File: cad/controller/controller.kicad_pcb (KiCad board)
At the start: 2 copper layers, 95 x 80 mm, 105 parts, among them J1 RJ45_jack_POE, J2 Barrel_Jack, J3 Conn_02x03_Odd_Even, J4 Conn_01x02, J5 Conn_01x04, J6 Conn_01x05, J7 6P6C, SW1 SW_Push, SW2 SW_Push, U1 NCP1117-5.0_SOT223, U2 NCP1117-3.3_SOT223, U3 CAT811STBI-GT3, U4 W5500, U5 ATmega328-PU, U6 PCA9517A, U7 TXB0104D, Y1 25MHz, Y2 18MHz

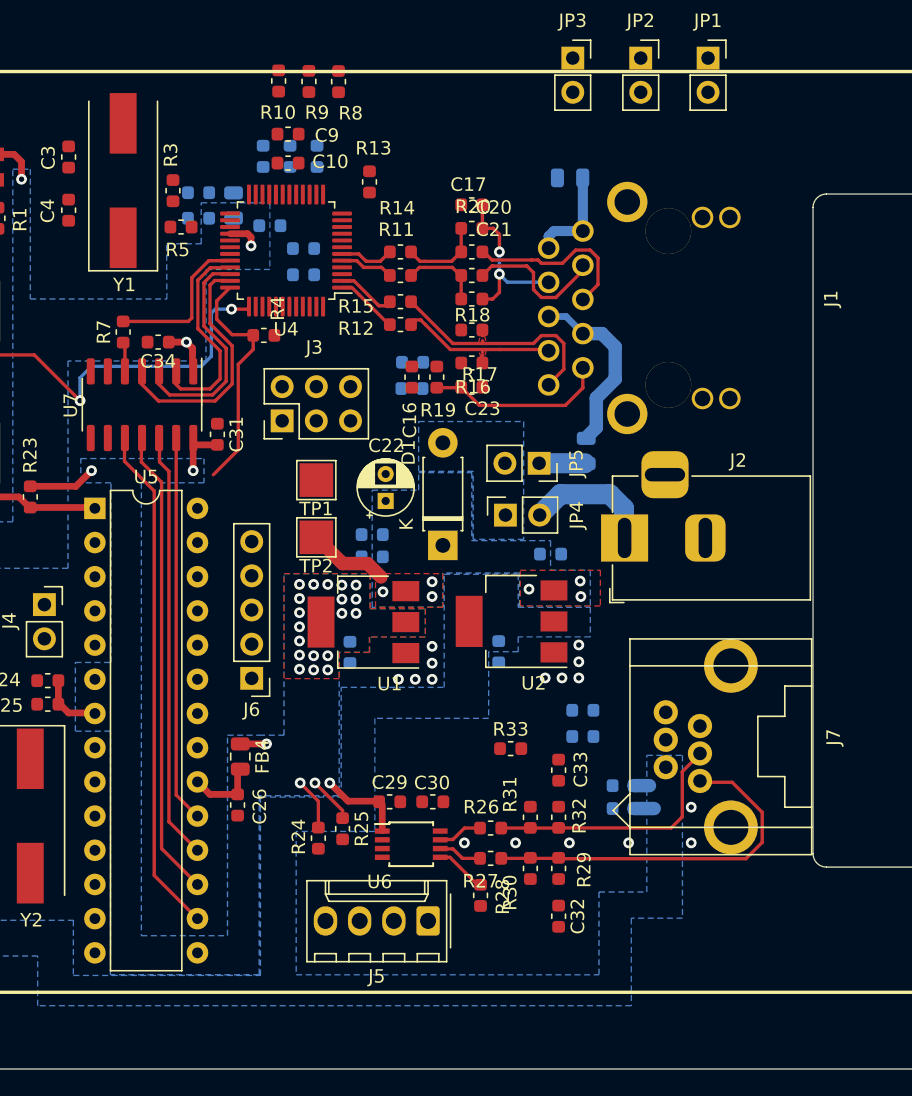
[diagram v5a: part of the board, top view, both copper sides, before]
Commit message: Continued routing controller board
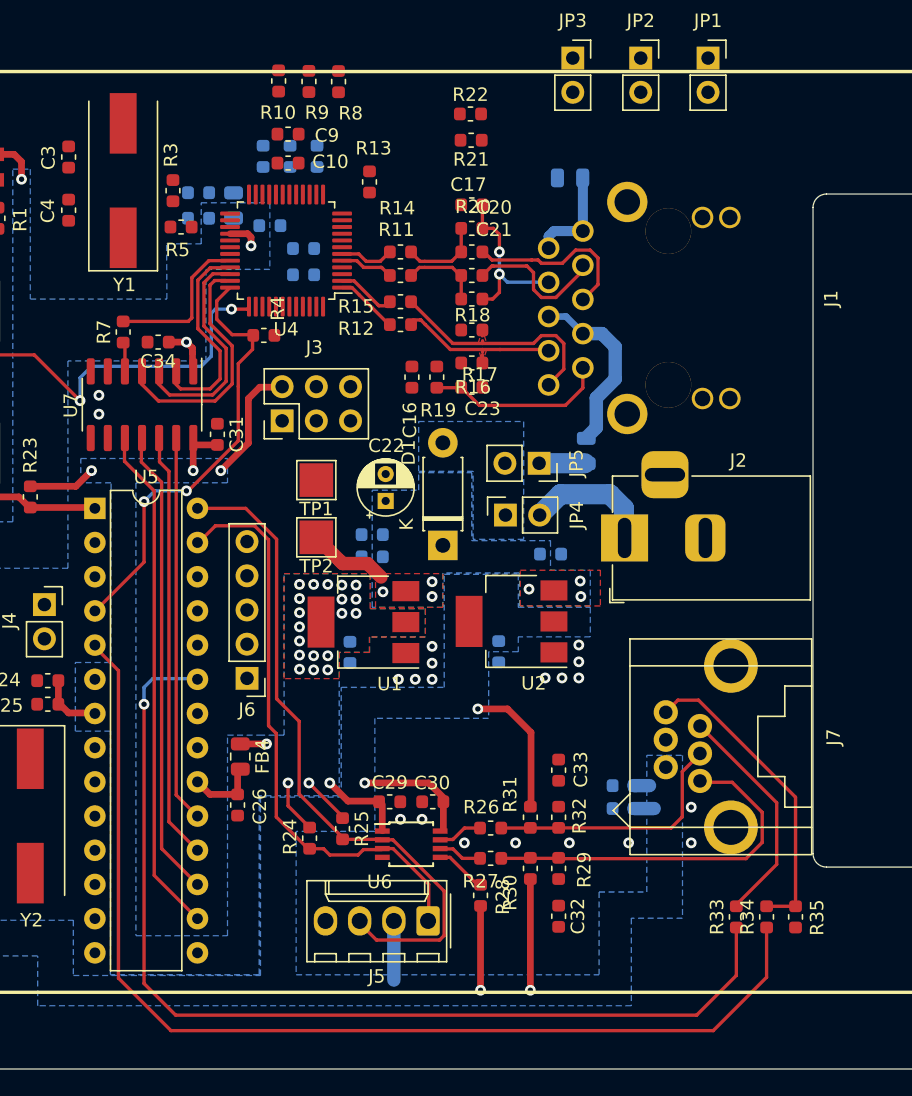
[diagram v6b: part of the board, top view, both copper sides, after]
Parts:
- R21, R22, R34, R35: moved to F.Cu
- moved R35 22.0 mm to (163.9, 113.0), turned to 90 degrees
- moved R33 20.9 mm to (159.6, 113.0), turned to 90 degrees
- moved R22 20.9 mm to (139.8, 53.4)
- moved R34 19.1 mm to (161.8, 113.0), turned to 90 degrees
- moved R21 17.1 mm to (139.8, 55.3)
- moved R24 0.65 mm to (127.8, 107.2)
- moved J6 0.35 mm to (123.2, 95.3)
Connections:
- R4 pad 1: /INT_W5500 -> INT_W5500
- U4 pad 36: /INT_W5500 -> INT_W5500
- U5 pad 4: /MCU/INT_W5500 -> INT_W5500
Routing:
- net /MCU/INT_SPARE: track 0.00 -> 80.6 mm
- net /MCU/ADC_0: track 0.00 -> 76.0 mm, vias 0 -> 1
- net /MCU/SCL: track 0.00 -> 50.2 mm
- net /MCU/SDA: track 0.00 -> 43.5 mm
- net 3V3: track 11.8 -> 49.7 mm, vias 3 -> 7
- net INT_W5500: track 0.00 -> 32.7 mm, vias 0 -> 2
- net Net-(J7-Pad1): track 0.00 -> 23.4 mm
- net /INT_W5500: track 17.5 -> 0.00 mm
- net Net-(J7-Pad2): track 0.00 -> 17.2 mm
- net 5V0: track 29.8 -> 39.1 mm, vias 25 -> 26
- net GND: vias 11 -> 13
- net (no net): vias 5 -> 7

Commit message: Continued routing controller
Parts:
- C16: moved to B.Cu
- moved J3 42.8 mm to (123.3, 118.8)
- moved C16 14.3 mm to (126.7, 61.6), turned to 0 degrees
- moved J5 5.28 mm to (140.2, 117.2)
- moved C8 2.76 mm to (123.8, 64.2), turned to 90 degrees
- moved R13 2.55 mm to (132.3, 61.0)
- moved C3 1.07 mm to (110.5, 57.5)
- moved R5 0.87 mm to (118.7, 62.5)
- moved C15 0.83 mm to (126.7, 65.0)
- moved R3 0.82 mm to (117.9, 59.9)
- moved Y1 0.81 mm to (114.2, 59.1)
- moved C14 0.75 mm to (126.7, 63.3)
- moved C11 0.60 mm to (124.4, 55.9)
- moved C12 0.60 mm to (126.4, 55.9)
- moved C13 0.60 mm to (128.4, 55.9)
- moved C10 0.55 mm to (126.2, 56.5)
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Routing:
- net RST: track 31.9 -> 83.2 mm
- net INT_W5500: track 32.7 -> 56.9 mm, vias 2 -> 0
- net /MCU/MOSI_5V: track 35.0 -> 54.3 mm
- net /3V3_ANA: track 0.00 -> 17.4 mm, vias 0 -> 8
- net /MCU/SCLK_5V: track 28.7 -> 45.7 mm
- net Net-(C3-Pad1): track 0.00 -> 16.9 mm
- net /MCU/MISO_5V: track 31.8 -> 44.6 mm
- net Net-(C4-Pad2): track 0.00 -> 11.7 mm
- net 5V0: track 39.1 -> 31.3 mm, vias 26 -> 25
- net /MCU/TX: track 0.00 -> 6.92 mm
- net /MCU/RX: track 0.00 -> 6.60 mm
- net /MCU/ADC_0: track 76.0 -> 82.4 mm
- net /MCU/SCL: track 50.2 -> 55.7 mm
- net /MCU/SDA: track 43.5 -> 48.5 mm
- net Net-(C9-Pad1): track 0.00 -> 4.99 mm
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- added copper zone on B.Cu, net /3V3_ANA

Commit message: Continued routing controller
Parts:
- moved JP2 30.2 mm to (122.2, 48.6)
- moved JP1 27.3 mm to (130.2, 48.6)
- moved R8 26.0 mm to (128.0, 76.8), turned to 180 degrees
- moved R21 24.7 mm to (149.0, 78.2)
- moved R9 24.3 mm to (126.7, 75.2), turned to 180 degrees
- moved R10 22.8 mm to (125.3, 73.7), turned to 180 degrees
- moved JP3 21.2 mm to (126.2, 48.6)
- moved R22 17.1 mm to (156.3, 57.9)
- moved R4 2.36 mm to (123.8, 72.0)
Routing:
- net Net-(JP1-Pad1): track 0.00 -> 78.7 mm, vias 0 -> 2
- net Net-(JP3-Pad1): track 0.00 -> 71.3 mm, vias 0 -> 2
- net Net-(JP2-Pad1): track 0.00 -> 64.0 mm, vias 0 -> 2
- net /LINK_LED: track 0.00 -> 42.0 mm
- net /ACT_LED: track 0.00 -> 39.7 mm, vias 0 -> 2
- net 3V3: track 46.6 -> 60.0 mm, vias 7 -> 8
- net Net-(J1-Pad13): track 0.00 -> 8.91 mm
- net Net-(J1-Pad11): track 0.00 -> 2.99 mm
- net INT_W5500: track 56.9 -> 55.8 mm
